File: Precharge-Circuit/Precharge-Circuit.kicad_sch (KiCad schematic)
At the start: 98 parts, among them J1 S2P-VH, J2 SM04B-PASS-1-TB, J3 SM02B-PASS-1-TB, J4 S2P-VH, J5 S2P-VH, J6 SM03B-PASS-1-TB, J7 19427-0040, J8 19427-0040, K1 G5Q-1A4_DC12, K2 AZDC6-2AE-12D, K3 G5Q-1A4_DC12, Q1 DMP3098LQ-7, Q10 2N7002K-AU, Q2 2N7002K-AU, Q3 PJA3439-AU_R1_000A1, Q4 2N7002K-AU, Q5 PJA3439-AU_R1_000A1, Q6 2N7002K-AU, Q7 PJA3439-AU_R1_000A1, Q8 2N7002K-AU, Q9 2N7002K-AU, U1 TLP291(GB,SE, U2 TLP291(GB,SE, U3 TL431QDBVR, U4 TL431QDBVR

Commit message: シンボル更新
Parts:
- C1, C3, C4: value 0.1u -> 0.1u_1608
- C2: value 10u -> 10u_3216
- C5: value 1000p -> 1000p_3216
- R1: value 100k -> 100k_1608
- R10, R11, R14, R20, R3, R6: value 1M -> 1M_1608
- R12, R18, R19, R27, R4, R7, R8, R9: value 10k -> 10k_1608
- R13, R15, R16, R17, R2, R5: value 100 -> 100_1608
- R21, R22, R23, R24, R25, R28, R29, R30, R31, R32: value 15k -> 15k_5025
- R26: value 1M -> 1M_3216
- R33, R34, R35, R36, R39, R40, R41, R42: value 1M -> 1M_5025
- R37: value 82k -> 82k_1608
- R38: value 13k -> 13k_1608
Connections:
- net TS-: no longer U3.6 (A), U3.7 (A), U4.6 (A), U4.7 (A)
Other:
- note added: "1 kV"

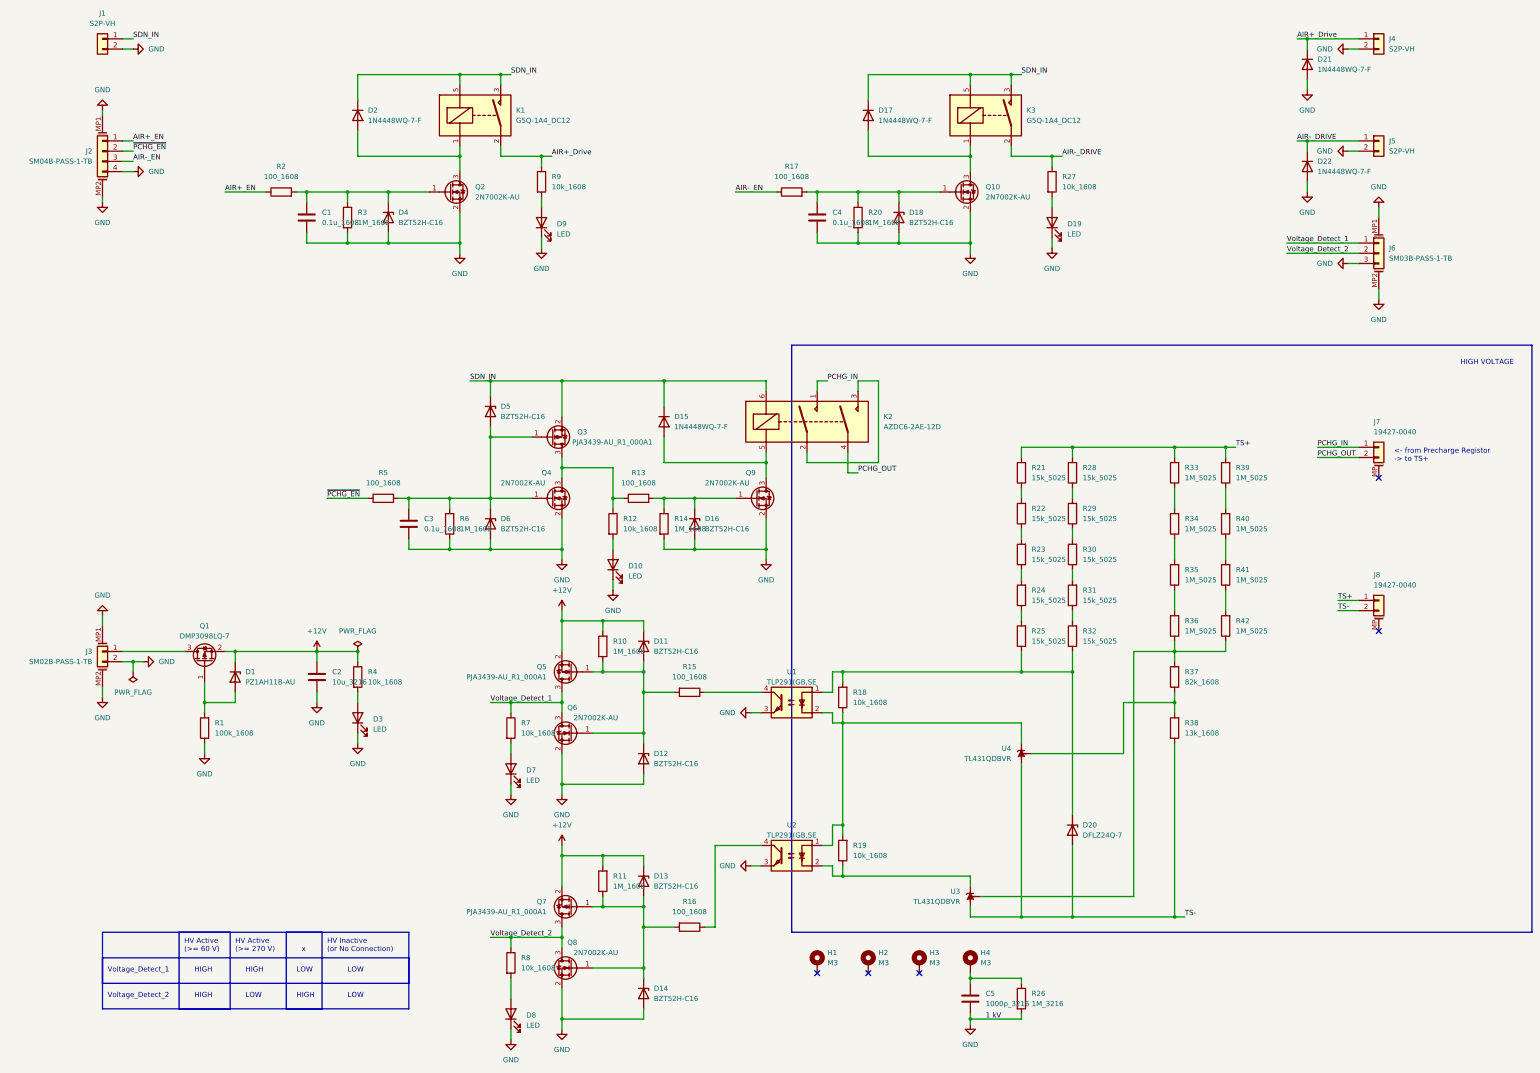
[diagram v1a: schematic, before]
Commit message: 位置修正、ツェナーの電流制限抵抗追加
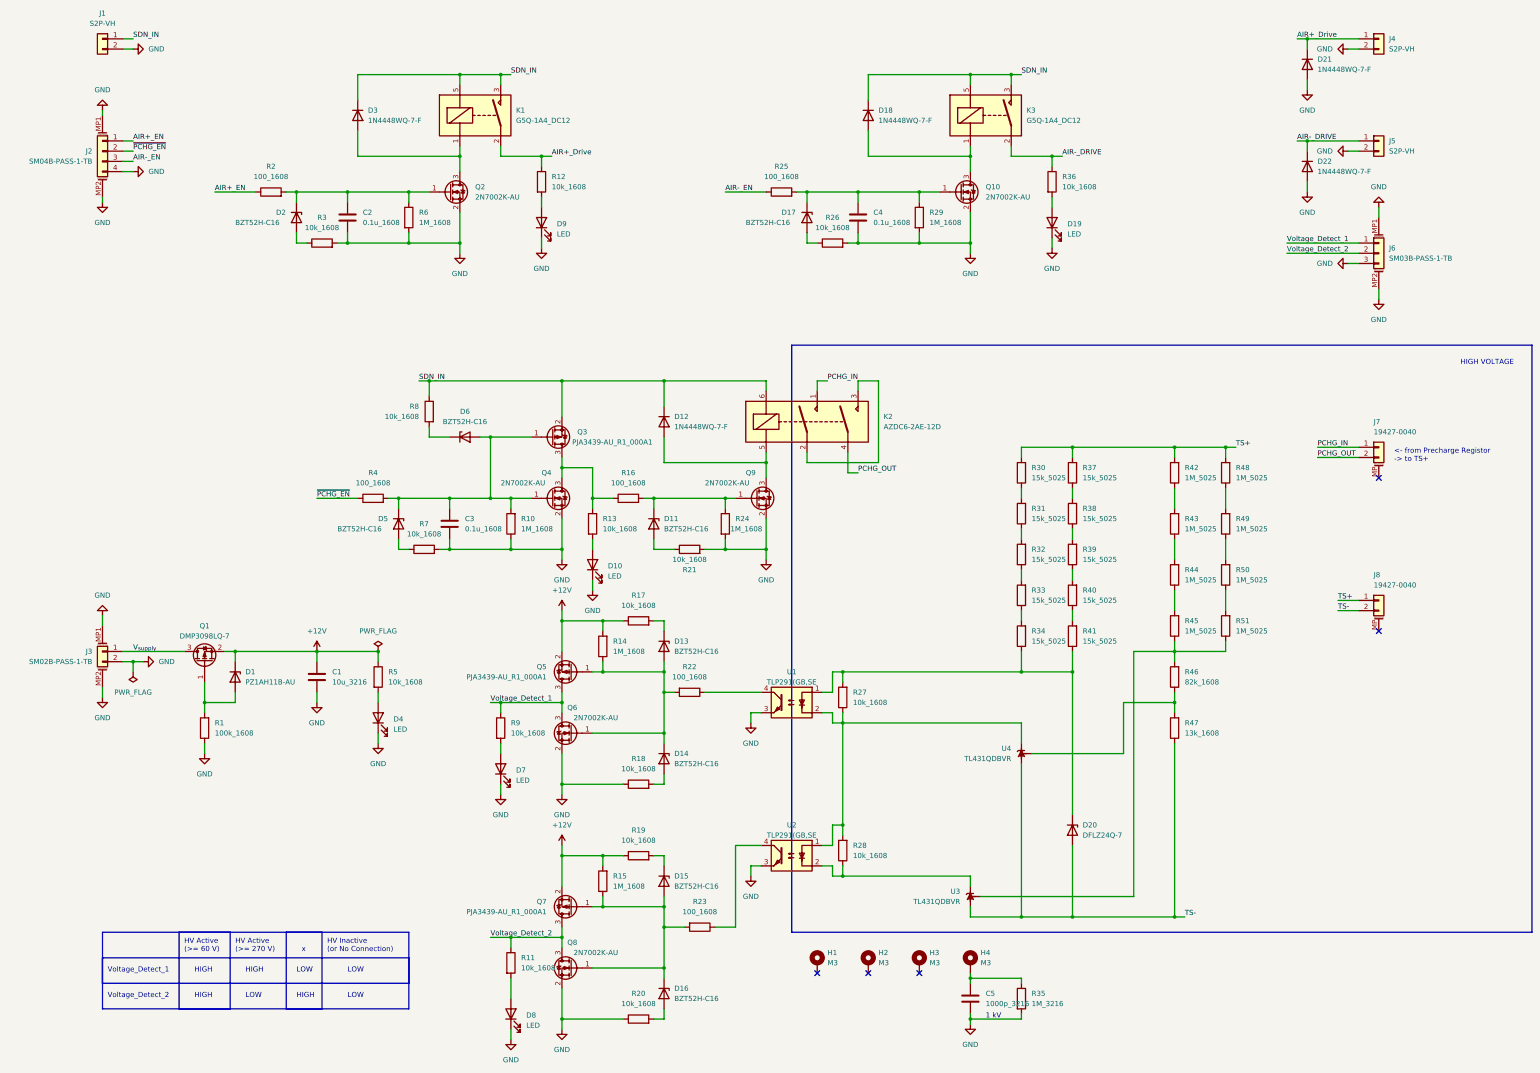
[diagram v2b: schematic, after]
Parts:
- added R17, R18, R19, R20, R21, R26, R3, R7, R8: 10k_1608, Resistor_SMD:R_0603_1608Metric, symbol Device:R
- renumbered C2 to C1, C1 to C2, D16 to D11, D15 to D12, D11 to D13, D12 to D14, D13 to D15, D14 to D16, D18 to D17, D17 to D18, D4 to D2, D2 to D3, D3 to D4, D6 to D5, D5 to D6, R6 to R10, R8 to R11, R9 to R12, R12 to R13, R10 to R14, R11 to R15, R13 to R16, R15 to R22, R16 to R23, R14 to R24, R17 to R25, R18 to R27, R19 to R28, R20 to R29, R21 to R30, R22 to R31, R23 to R32, R24 to R33, R25 to R34, R26 to R35, R27 to R36, R28 to R37, R29 to R38, R30 to R39, R5 to R4, R31 to R40, R32 to R41, R33 to R42, R34 to R43, R35 to R44, R36 to R45, R37 to R46, R38 to R47, R39 to R48, R40 to R49, R4 to R5, R41 to R50, R42 to R51, R3 to R6, R7 to R9
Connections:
- net +12V: now also R17.1, R19.1; no longer D13.1 (K), D15.1 (K)
- net GND: now also R18.1, R20.1, R21.2, R26.2, R3.2, R7.2; no longer D11.2 (A), D14.2 (A), D16.2 (A), D17.2 (A), D2.2 (A), D5.2 (A)
- net SDN_IN: now also R8.1; no longer D6.1 (K)
- net V_{supply}: now reaches J3.1 (Pin_1), Q1.3 (D)
- new net: D16.2 (A), R20.2
- new net: D14.2 (A), R18.2
- new net: D17.2 (A), R26.1
- new net: D15.1 (K), R19.2
- new net: D6.1 (K), R8.2
- new net: D11.2 (A), R21.1
- new net: D5.2 (A), R7.1
- new net: D13.1 (K), R17.2
- new net: D2.2 (A), R3.1
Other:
- moved on the sheet: C2, C3, C4, D10, D11, D13, D14, D15, D16, D17, D2, D4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

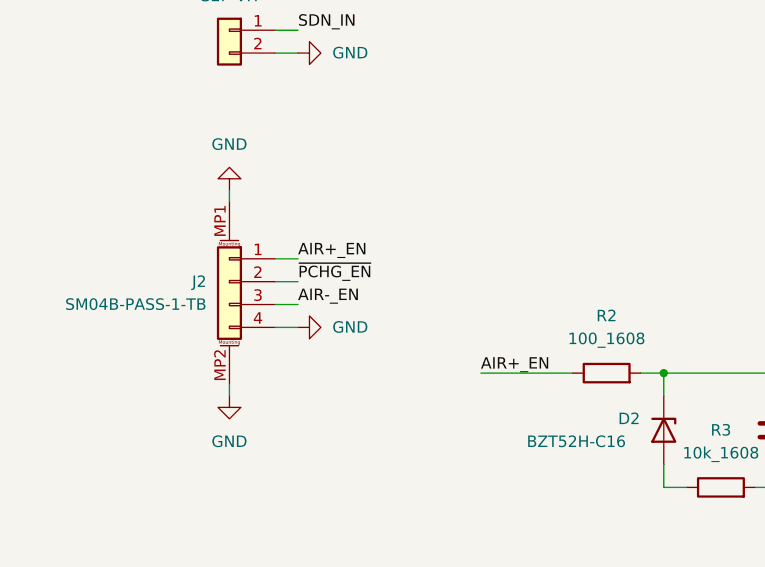
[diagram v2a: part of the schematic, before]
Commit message: パーツ配置、ピンアサイン変更
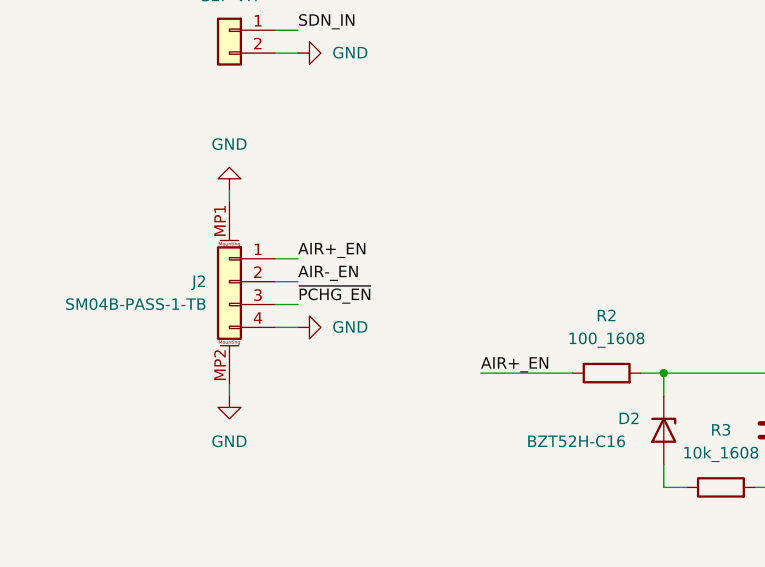
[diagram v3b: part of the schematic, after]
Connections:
- net AIR-_EN: now also J2.2 (Pin_2); no longer J2.3 (Pin_3)
- net ~{PCHG_EN}: now also J2.3 (Pin_3); no longer J2.2 (Pin_2)

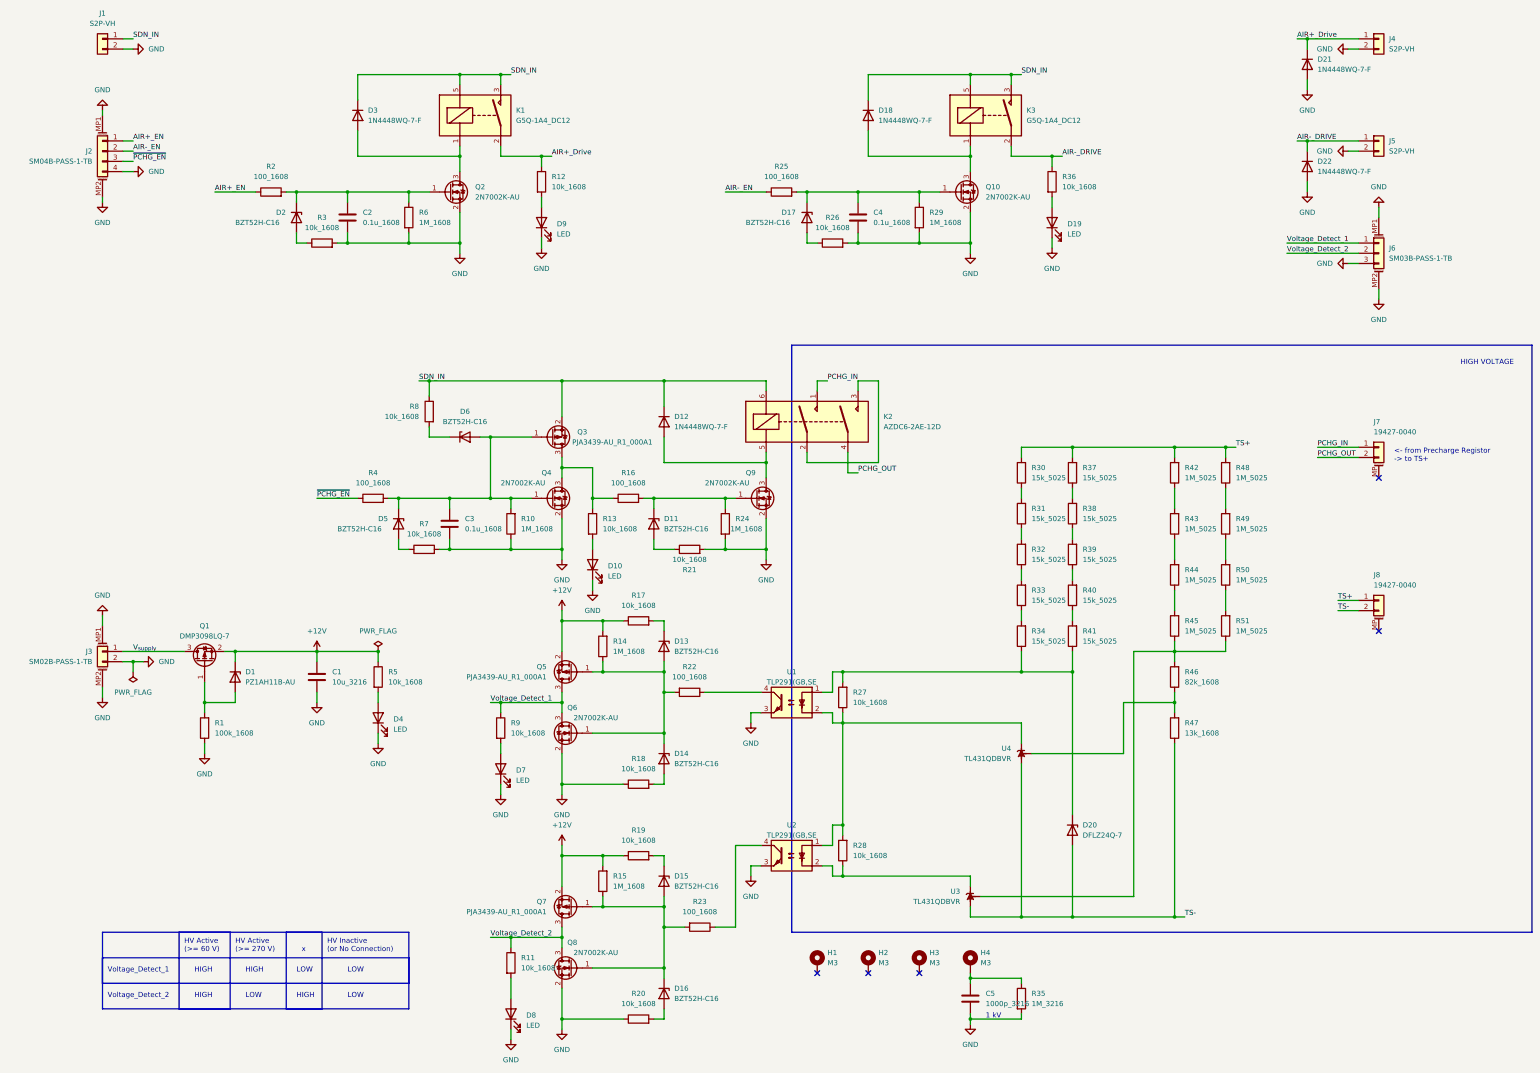
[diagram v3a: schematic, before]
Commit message: NOT ゲートの電流制限抵抗追加、高電圧コネクタフットプリント更新、配線GNDベタ以外
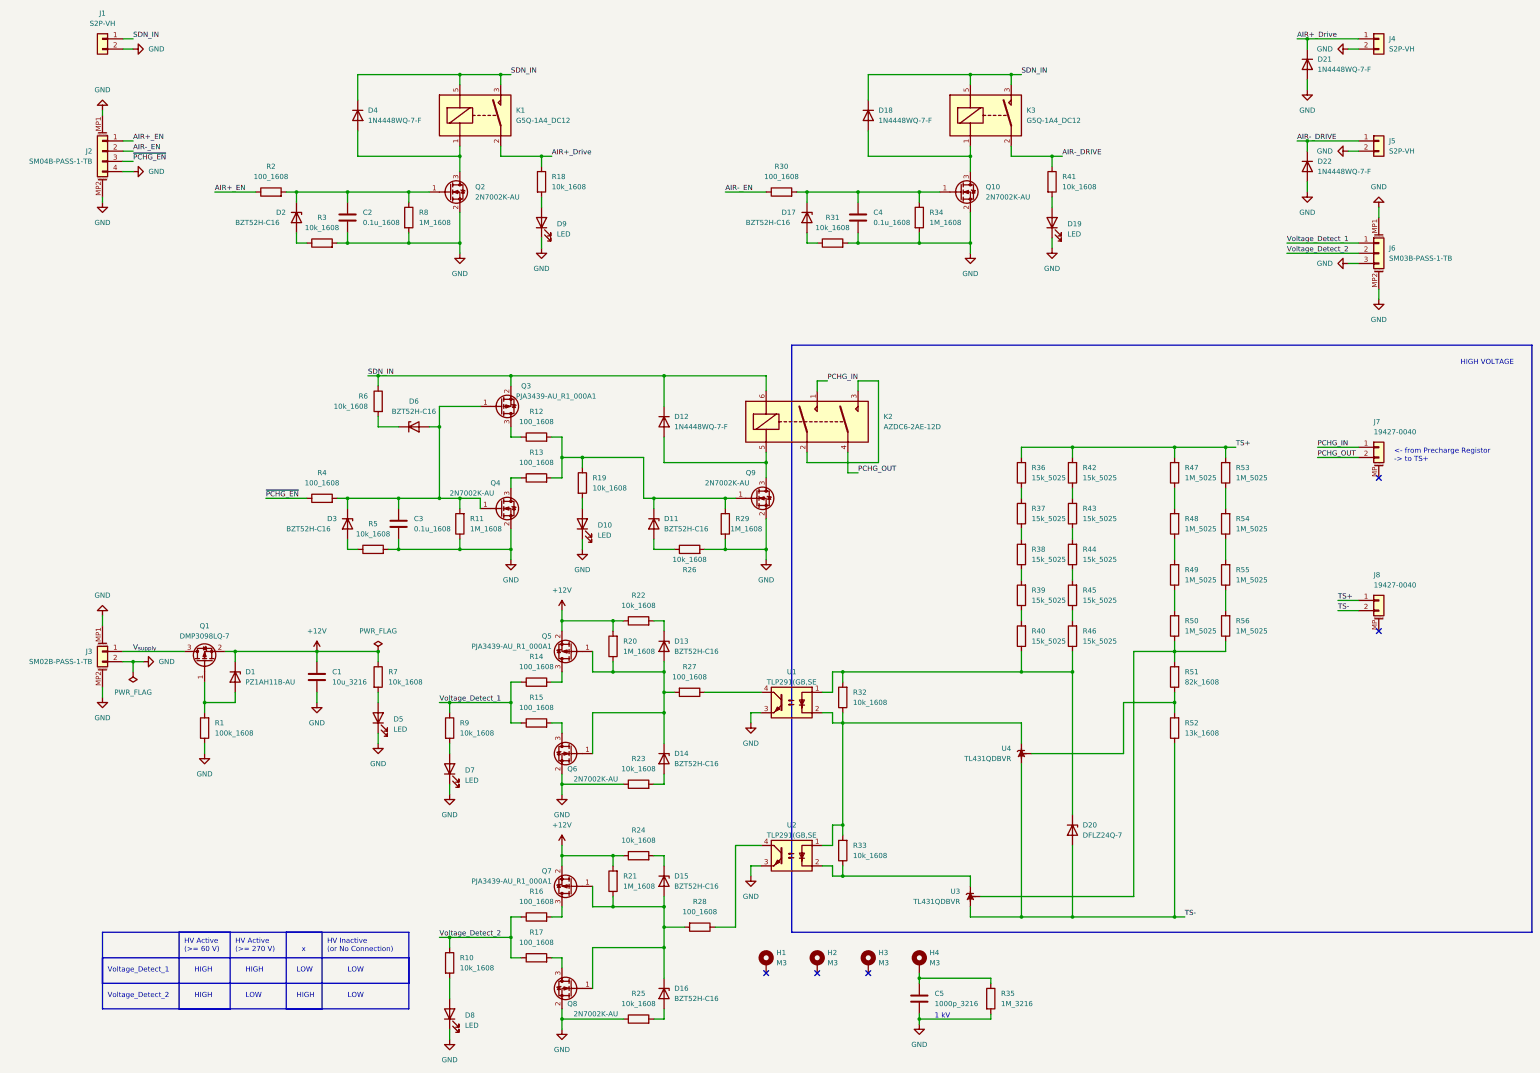
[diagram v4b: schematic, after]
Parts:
- added R13, R14, R15, R16, R17: 100_1608, Resistor_SMD:R_0603_1608Metric, symbol Device:R
- renumbered D5 to D3, D3 to D4, D4 to D5, R11 to R10, R10 to R11, R16 to R12, R12 to R18, R13 to R19, R14 to R20, R15 to R21, R17 to R22, R18 to R23, R19 to R24, R20 to R25, R21 to R26, R22 to R27, R23 to R28, R24 to R29, R25 to R30, R26 to R31, R27 to R32, R28 to R33, R29 to R34, R30 to R36, R31 to R37, R32 to R38, R33 to R39, R34 to R40, R36 to R41, R37 to R42, R38 to R43, R39 to R44, R40 to R45, R41 to R46, R42 to R47, R43 to R48, R44 to R49, R7 to R5, R45 to R50, R46 to R51, R47 to R52, R48 to R53, R49 to R54, R50 to R55, R51 to R56, R8 to R6, R5 to R7, R6 to R8
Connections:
- net Voltage_Detect_1: now also R14.1, R15.1; no longer Q5.3 (D), Q6.3 (D)
- net Voltage_Detect_2: now also R16.1, R17.1; no longer Q7.3 (D), Q8.3 (D)
- net at D11.1 (K), Q9.1 (G), R12.2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: now also R19.1, R13.2
- net at Q3.3 (D), R12.1: no longer Q4.3 (D), R19.1
- new net: Q8.3 (D), R17.2
- new net: Q7.3 (D), R16.2
- new net: Q6.3 (D), R15.2
- new net: Q4.3 (D), R13.1
- new net: Q5.3 (D), R14.2
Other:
- moved on the sheet: C3, C5, D10, D3, D6, D7, D8, H1, H2, H3, H4, Q3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
